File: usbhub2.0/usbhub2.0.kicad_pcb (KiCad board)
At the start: 2 copper layers, 75 x 35 mm, 31 parts, among them J1 Conn_01x05_Male, J2 Conn_01x05_Male, J4 Conn_01x05_Male, J5 USB_InputPort, J7 Conn_01x05_Male, J9 Power, U1 FE1.1s, Y1 Crystal_12MHz

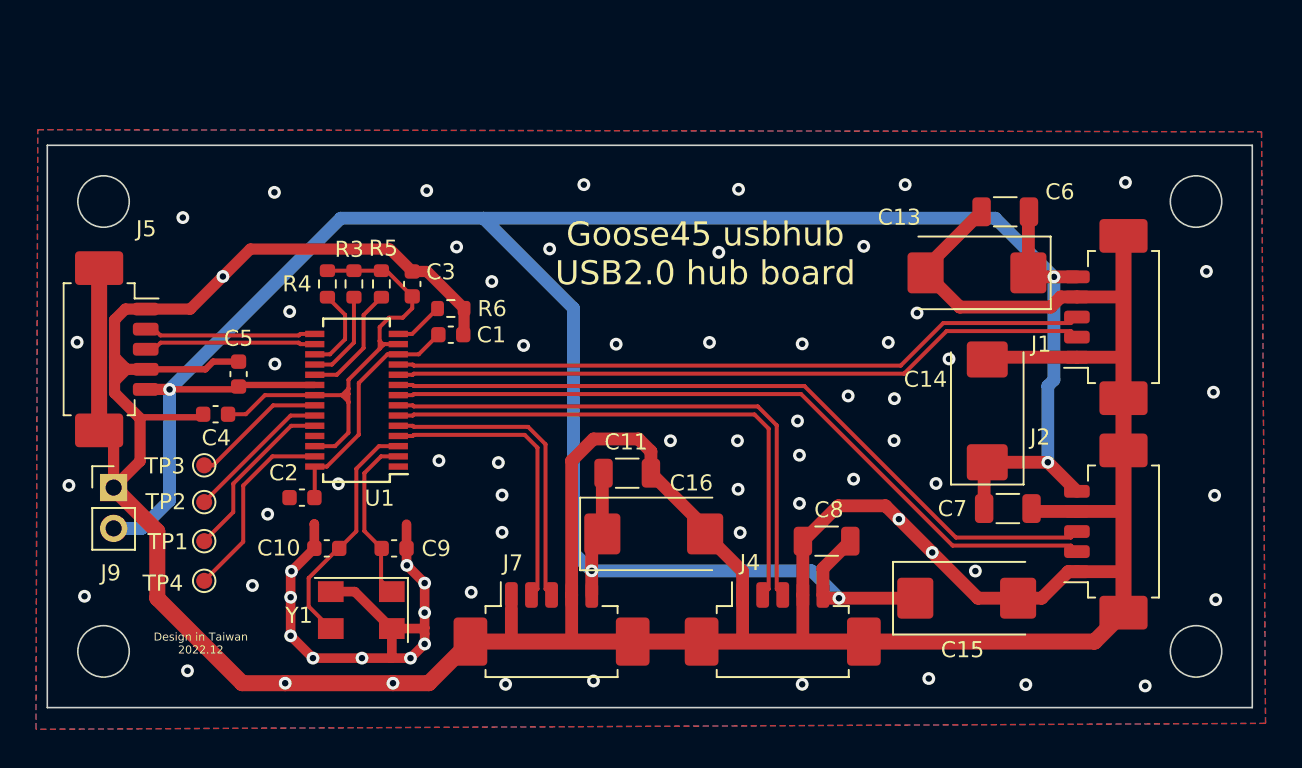
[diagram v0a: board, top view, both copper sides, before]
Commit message: change usbhub2.0 board design
* remove usb molex input and add usb-c to input channel
* change usbout1 molex to pin header
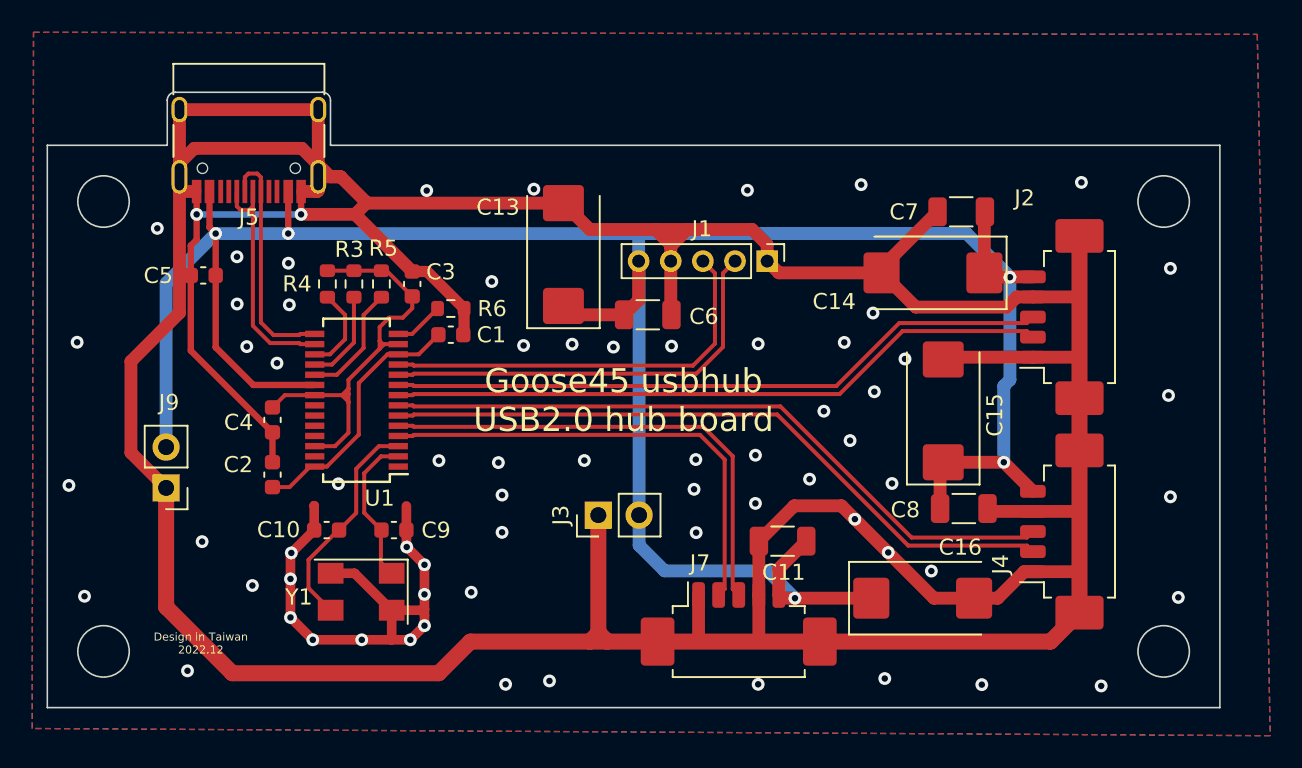
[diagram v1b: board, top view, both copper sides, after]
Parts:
- removed TP1, TP2, TP3, TP4: TestPoint, TestPoint:TestPoint_Pad_D1.0mm
- added J3: Power, Connector_PinHeader_2.54mm:PinHeader_1x02_P2.54mm_Vertical, F.Cu at (125.8, 105.6)
- J1: footprint Connector_Molex:Molex_PicoBlade_53261-0571_1x05-1MP_P1.25mm_Horizontal -> Connector_PinHeader_2.00mm:PinHeader_1x05_P2.00mm_Vertical
- J5: value USB_InputPort -> USB_C_Receptacle_USB2.0; footprint Connector_Molex:Molex_PicoBlade_53261-0571_1x05-1MP_P1.25mm_Horizontal -> Connector_USB:USB_C_Receptacle_HRO_TYPE-C-31-M-12
- moved C13 25.8 mm to (123.6, 89.4), turned to 90 degrees
- moved C6 23.2 mm to (128.9, 93.2), turned to 0 degrees
- moved J1 22.0 mm to (136.3, 89.8), turned to -90 degrees
- moved J4 19.1 mm to (155.3, 106.7), turned to 90 degrees
- moved C7 18.7 mm to (148.4, 86.8), turned to 180 degrees
- moved C16 17.2 mm to (146.0, 110.8)
- moved J5 16.4 mm to (104.1, 81.4), turned to 180 degrees
- moved J2 13.6 mm to (155.3, 93.3)
- moved C15 11.8 mm to (147.3, 99.1), turned to 90 degrees
- moved J7 11.7 mm to (134.6, 113.0)
- moved C11 10.6 mm to (137.3, 107.2), turned to 180 degrees
- moved C14 9.23 mm to (146.6, 90.5), turned to 180 degrees
- moved C8 8.78 mm to (148.6, 105.2), turned to 0 degrees
- moved C5 6.52 mm to (101.2, 90.7), turned to 180 degrees
- moved C4 3.56 mm to (105.5, 99.7), turned to -90 degrees
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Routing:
- net GND: track 291.3 -> 341.9 mm, vias 71 -> 69
- net USB1_D+: track 43.5 -> 25.8 mm
- net USB1_D-: track 43.5 -> 26.6 mm
- net EESDA: track 12.1 -> 0.00 mm
- net USB4_D-: track 18.3 -> 29.6 mm
- net USB4_D+: track 19.2 -> 30.4 mm
- net LED2: track 10.9 -> 0.00 mm
- net LED1: track 9.12 -> 0.00 mm
- net USB3_D-: track 34.0 -> 43.1 mm
- net VIN: track 169.3 -> 160.8 mm
- net DRV: track 8.43 -> 0.00 mm
- net USB3_D+: track 34.8 -> 43.1 mm
- net USB_D+: track 10.2 -> 16.0 mm
- net USB2_D+: track 46.3 -> 41.3 mm
- net USB2_D-: track 46.3 -> 41.3 mm
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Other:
- board size 75 x 35 mm -> 73 x 38.3 mm

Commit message: update goose45 pcb board edge comment
* goose45 - update board layout
* usbport - change edge size and add edge comment
* usbhub2.0 - change layout and the footprint
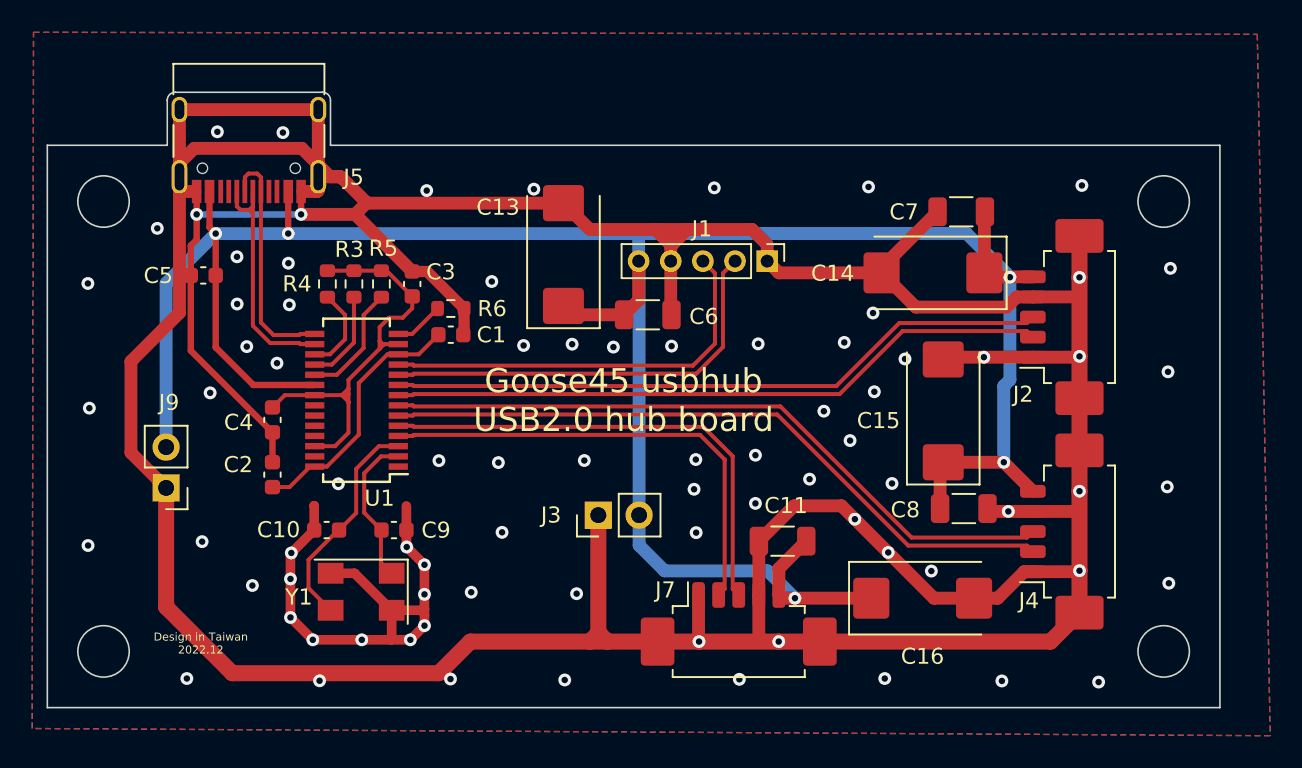
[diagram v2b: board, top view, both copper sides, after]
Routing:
- net GND: vias 69 -> 81
